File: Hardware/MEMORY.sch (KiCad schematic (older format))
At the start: 9 parts, among them J37 Micro_SD_Card, U20 M24C64-WDW6TP

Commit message: Fixed merge issues
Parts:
- renumbered J37 to J14, R41 to R24, R42 to R25, R43 to R26, R44 to R27, R45 to R28, R46 to R29, R47 to R30, U20 to U11
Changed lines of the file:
@@
 LIBS:contrib
 LIBS:valves
+LIBS:ZeroPilot-cache
 EELAYER 25 0
 EELAYER END
@@
 $EndDescr
 $Comp
-L GND #PWR43
+L GND #PWR036
 U 1 1 5920672F
 P 9150 2600
-F 0 "#PWR43" H 9150 2350 50  0001 C CNN
+F 0 "#PWR036" H 9150 2350 50  0001 C CNN
 F 1 "GND" H 9150 2450 50  0000 C CNN
 F 2 "" H 9150 2600 50  0001 C CNN
@@
 SD_CS
 $Comp
-L GND #PWR42
+L GND #PWR037
 U 1 1 592067B5
 P 7300 2400
-F 0 "#PWR42" H 7300 2150 50  0001 C CNN
+F 0 "#PWR037" H 7300 2150 50  0001 C CNN
 F 1 "GND" H 7300 2250 50  0000 C CNN
 F 2 "" H 7300 2400 50  0001 C CNN
@@
 $EndComp
 $Comp
-L GND #PWR41
+L GND #PWR038
 U 1 1 592069E4
 P 5150 5850
-F 0 "#PWR41" H 5150 5600 50  0001 C CNN
+F 0 "#PWR038" H 5150 5600 50  0001 C CNN
 F 1 "GND" H 5150 5700 50  0000 C CNN
 F 2 "" H 5150 5850 50  0001 C CNN
@@
 E3
 $Comp
-L R R42
+L R R25
 U 1 1 59206C6F
 P 1650 5650
-F 0 "R42" V 1730 5650 50  0000 C CNN
+F 0 "R25" V 1730 5650 50  0000 C CNN
 F 1 "10K" V 1650 5650 50  0000 C CNN
 F 2 "Resistors_SMD:R_0603_HandSoldering" V 1580 5650 50  0001 C CNN
@@
 $EndComp
 $Comp
-L R R41
+L R R24
 U 1 1 59206D63
 P 1650 5100
-F 0 "R41" V 1730 5100 50  0000 C CNN
+F 0 "R24" V 1730 5100 50  0000 C CNN
 F 1 "0" V 1650 5100 50  0000 C CNN
 F 2 "Resistors_SMD:R_0603_HandSoldering" V 1580 5100 50  0001 C CNN
@@
 $EndComp
 $Comp
-L GND #PWR40
+L GND #PWR039
 U 1 1 59206DDE
 P 1900 5950
-F 0 "#PWR40" H 1900 5700 50  0001 C CNN
+F 0 "#PWR039" H 1900 5700 50  0001 C CNN
 F 1 "GND" H 1900 5800 50  0000 C CNN
 F 2 "" H 1900 5950 50  0001 C CNN
@@
 NoConn ~ 7400 2300
 $Comp
-L Micro_SD_Card J37
+L Micro_SD_Card J14
 U 1 1 59517B7C
 P 8300 1900
-F 0 "J37" H 7650 2500 50  0000 C CNN
+F 0 "J14" H 7650 2500 50  0000 C CNN
 F 1 "Micro_SD_Card" H 8950 2500 50  0000 R CNN
 F 2 "WARG:micro_sd" H 9450 2200 50  0001 C CNN
@@
 $EndComp
 $Comp
-L R R44
+L R R27
 U 1 1 59596B34
 P 1900 5650
-F 0 "R44" V 1980 5650 50  0000 C CNN
+F 0 "R27" V 1980 5650 50  0000 C CNN
 F 1 "10K" V 1900 5650 50  0000 C CNN
 F 2 "Resistors_SMD:R_0603_HandSoldering" V 1830 5650 50  0001 C CNN
@@
 $EndComp
 $Comp
-L R R46
+L R R29
 U 1 1 59596B68
 P 2150 5650
-F 0 "R46" V 2230 5650 50  0000 C CNN
+F 0 "R29" V 2230 5650 50  0000 C CNN
 F 1 "10K" V 2150 5650 50  0000 C CNN
 F 2 "Resistors_SMD:R_0603_HandSoldering" V 2080 5650 50  0001 C CNN
@@
 $EndComp
 $Comp
-L R R43
+L R R26
 U 1 1 59596BE6
 P 1900 5100
-F 0 "R43" V 1980 5100 50  0000 C CNN
+F 0 "R26" V 1980 5100 50  0000 C CNN
 F 1 "0" V 1900 5100 50  0000 C CNN
 F 2 "Resistors_SMD:R_0603_HandSoldering" V 1830 5100 50  0001 C CNN
@@
 $EndComp
 $Comp
-L R R45
+L R R28
 U 1 1 59596C1A
 P 2150 5100
-F 0 "R45" V 2230 5100 50  0000 C CNN
+F 0 "R28" V 2230 5100 50  0000 C CNN
 F 1 "0" V 2150 5100 50  0000 C CNN
 F 2 "Resistors_SMD:R_0603_HandSoldering" V 2080 5100 50  0001 C CNN
@@
 $EndComp
 $Comp
-L R R47
+L R R30
 U 1 1 59596D32
 P 3950 5300
-F 0 "R47" V 4030 5300 50  0000 C CNN
+F 0 "R30" V 4030 5300 50  0000 C CNN
 F 1 "10K" V 3950 5300 50  0000 C CNN
 F 2 "Resistors_SMD:R_0603_HandSoldering" V 3880 5300 50  0001 C CNN
@@
 $EndComp
 $Comp
-L M24C64-WDW6TP U20
+L M24C64-WDW6TP U11
 U 1 1 595FB585
 P 5300 5000
-F 0 "U20" H 5300 5450 60  0000 C CNN
+F 0 "U11" H 5300 5450 60  0000 C CNN
 F 1 "M24C64-WDW6TP" H 5250 4100 60  0000 C CNN
 F 2 "Housings_SSOP:TSSOP-8_4.4x3mm_Pitch0.65mm" H 5200 5350 60  0001 C CNN

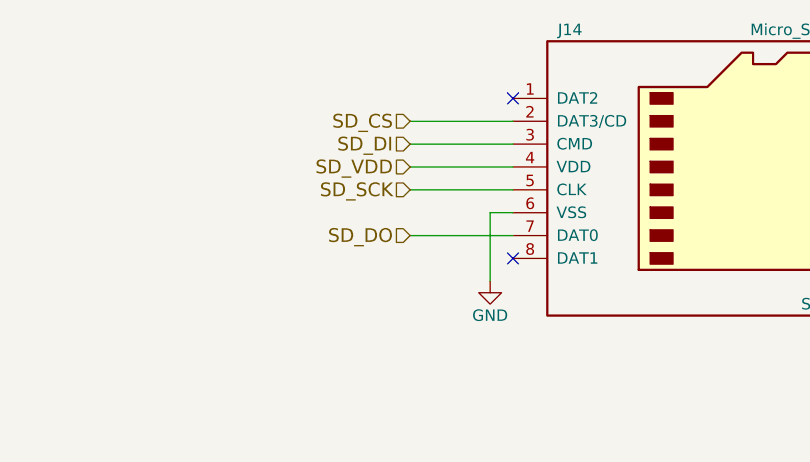
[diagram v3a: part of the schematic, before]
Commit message: Updated schematic
-Changed diode to 0603 diodes
-Changed SD card to proper pinout
-Fixed SPI1 conflict
-Renamed some power nets
-Fixed naming error in IMU NSS
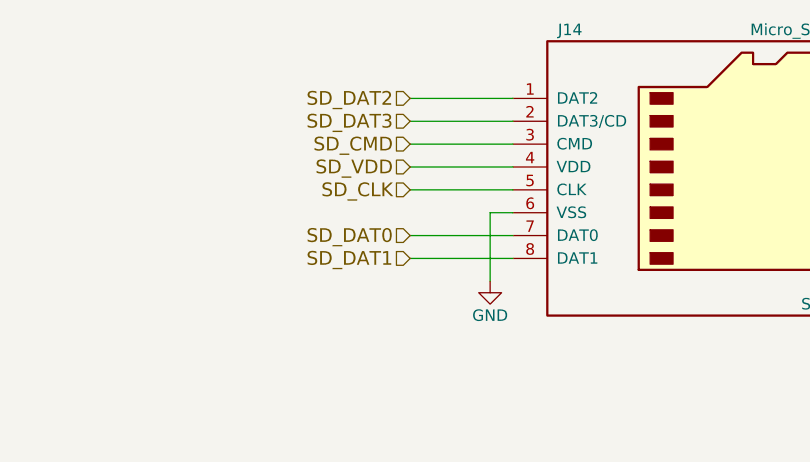
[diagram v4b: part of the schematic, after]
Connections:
- net labels added: SD_CLK, SD_CMD, SD_DAT0, SD_DAT1, SD_DAT2, SD_DAT3
- net labels removed: SD_CS, SD_DI, SD_DO, SD_SCK
- wire segments 28 -> 30
- no-connect marks 2 -> 0
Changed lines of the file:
@@
 $EndComp
 Text HLabel 6950 1800 0    60   Input ~ 0
-SD_DI
+SD_CMD
 Text HLabel 6950 2200 0    60   Input ~ 0
-SD_DO
+SD_DAT0
 Text HLabel 6950 2000 0    60   Input ~ 0
-SD_SCK
+SD_CLK
 Text HLabel 6950 1900 0    60   Input ~ 0
 SD_VDD
 Text HLabel 6950 1700 0    60   Input ~ 0
-SD_CS
+SD_DAT3
 $Comp
 L GND #PWR037
@@
 Text Notes 1250 4650 0    60   ~ 0
 Populate resistors to select I2C address\n
-NoConn ~ 7400 1600
-NoConn ~ 7400 2300
 $Comp
 L Micro_SD_Card J14
@@
 Text HLabel 3850 5500 0    60   Input ~ 0
 WC
+Wire Wire Line
+	7400 2300 6950 2300
+Text HLabel 6950 2300 0    60   Input ~ 0
+SD_DAT1
+Text HLabel 6950 1600 0    60   Input ~ 0
+SD_DAT2
+Wire Wire Line
+	6950 1600 7400 1600
 $EndSCHEMATC

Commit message: Remapped symbols for KiCAD 5.0.x
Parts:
- J14: symbol Micro_SD_Card -> conn:Micro_SD_Card
- R24, R25, R26, R27, R28, R29, R30: symbol R -> Device:R
- U11: symbol M24C64-WDW6TP -> WARG:M24C64-WDW6TP
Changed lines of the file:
@@
-EESchema Schematic File Version 2
-LIBS:WARG
-LIBS:power
-LIBS:device
-LIBS:transistors
-LIBS:conn
-LIBS:linear
-LIBS:regul
-LIBS:74xx
-LIBS:cmos4000
-LIBS:adc-dac
-LIBS:memory
-LIBS:xilinx
-LIBS:microcontrollers
-LIBS:dsp
-LIBS:microchip
-LIBS:analog_switches
-LIBS:motorola
-LIBS:texas
-LIBS:intel
-LIBS:audio
-LIBS:interface
-LIBS:digital-audio
-LIBS:philips
-LIBS:display
-LIBS:cypress
-LIBS:siliconi
-LIBS:opto
-LIBS:atmel
-LIBS:contrib
-LIBS:valves
+EESchema Schematic File Version 4
 LIBS:ZeroPilot-cache
-EELAYER 25 0
+EELAYER 26 0
 EELAYER END
 $Descr A4 11693 8268
@@
 $EndDescr
 $Comp
-L GND #PWR036
+L power:GND #PWR036
 U 1 1 5920672F
 P 9150 2600
@@
 SD_DAT3
 $Comp
-L GND #PWR037
+L power:GND #PWR037
 U 1 1 592067B5
 P 7300 2400
@@
 $EndComp
 $Comp
-L GND #PWR038
+L power:GND #PWR038
 U 1 1 592069E4
 P 5150 5850
@@
 E3
 $Comp
-L R R25
+L Device:R R25
 U 1 1 59206C6F
 P 1650 5650
@@
 $EndComp
 $Comp
-L R R24
+L Device:R R24
 U 1 1 59206D63
 P 1650 5100
@@
 $EndComp
 $Comp
-L GND #PWR039
+L power:GND #PWR039
 U 1 1 59206DDE
 P 1900 5950
@@
 Populate resistors to select I2C address\n
 $Comp
-L Micro_SD_Card J14
+L conn:Micro_SD_Card J14
 U 1 1 59517B7C
 P 8300 1900
@@
 $EndComp
 $Comp
-L R R27
+L Device:R R27
 U 1 1 59596B34
 P 1900 5650
@@
 $EndComp
 $Comp
-L R R29
+L Device:R R29
 U 1 1 59596B68
 P 2150 5650
@@
 $EndComp
 $Comp
-L R R26
+L Device:R R26
 U 1 1 59596BE6
 P 1900 5100
@@
 $EndComp
 $Comp
-L R R28
+L Device:R R28
 U 1 1 59596C1A
 P 2150 5100
@@
 $EndComp
 $Comp
-L R R30
+L Device:R R30
 U 1 1 59596D32
 P 3950 5300
@@
 $EndComp
 $Comp
-L M24C64-WDW6TP U11
+L WARG:M24C64-WDW6TP U11
 U 1 1 595FB585
 P 5300 5000
@@
 	5550 5350 5750 5350
 Wire Wire Line
-	3850 5500 4650 5500
+	3850 5500 3950 5500
 Wire Wire Line
 	3950 5450 3950 5500
@@
 	1650 5800 1650 5900
 Wire Wire Line
-	1650 5900 2150 5900
+	1650 5900 1900 5900
 Wire Wire Line
 	2150 5900 2150 5800
 Wire Wire Line
-	1900 5800 1900 5950
+	1900 5800 1900 5900
 Connection ~ 1900 5900
 Wire Wire Line
-	1650 4800 2150 4800
+	1650 4800 1900 4800
 Wire Wire Line
 	1650 4800 1650 4950
@@
 Wire Wire Line
 	6950 1600 7400 1600
+Wire Wire Line
+	3950 5500 4650 5500
+Wire Wire Line
+	1900 5900 2150 5900
+Wire Wire Line
+	1900 5900 1900 5950
+Wire Wire Line
+	1900 4800 2150 4800
 $EndSCHEMATC

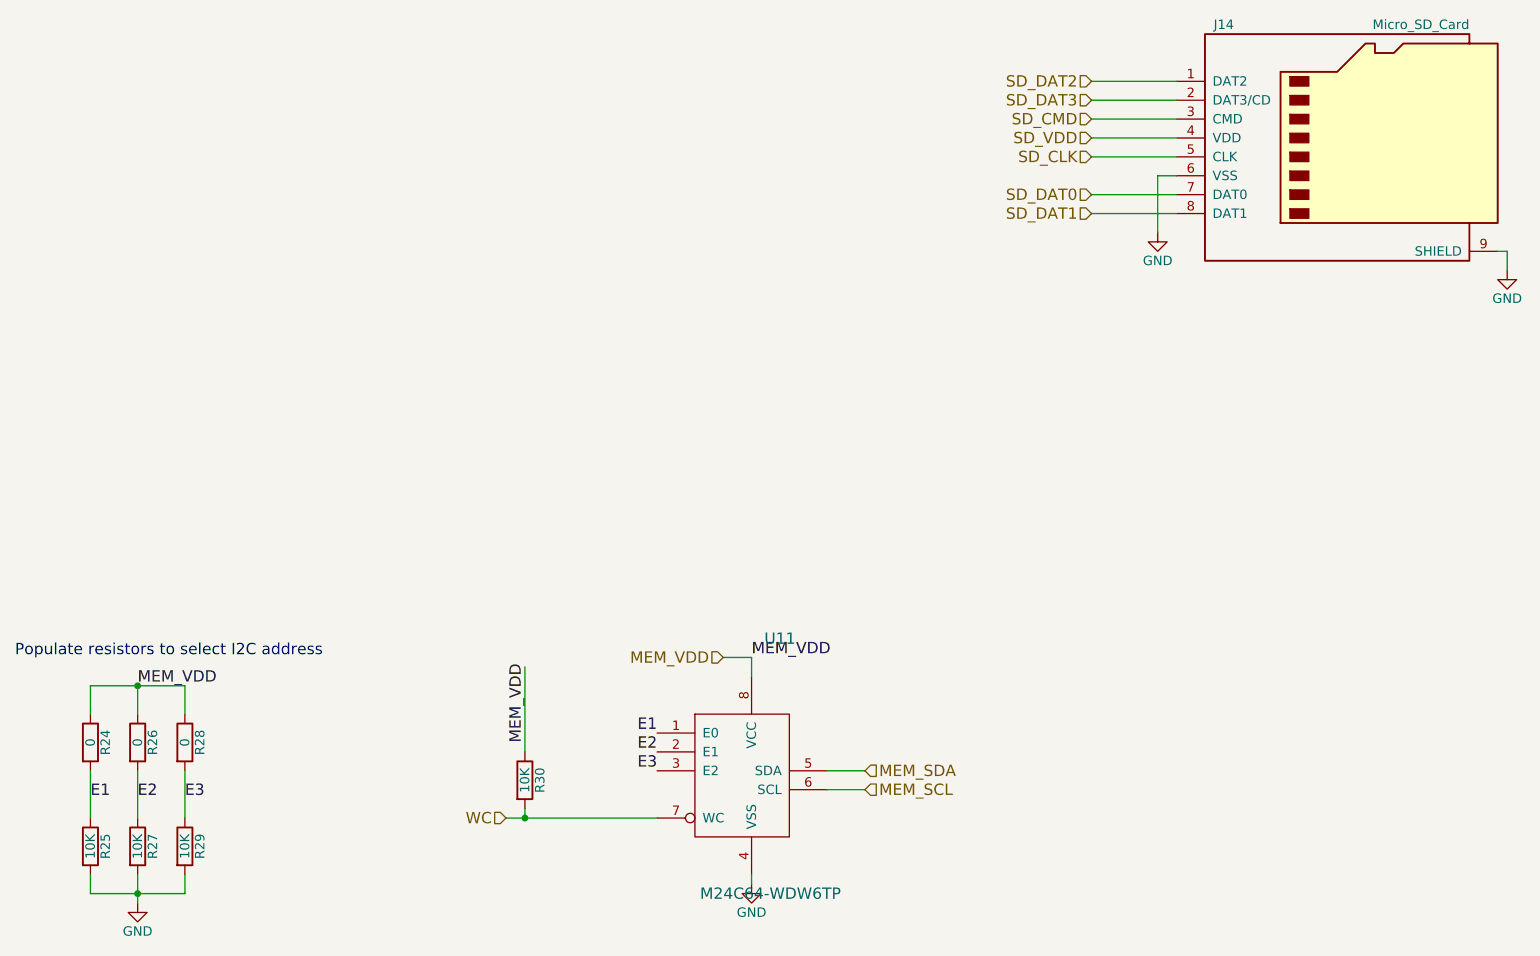
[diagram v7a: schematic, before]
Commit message: Generated netlist and board outline
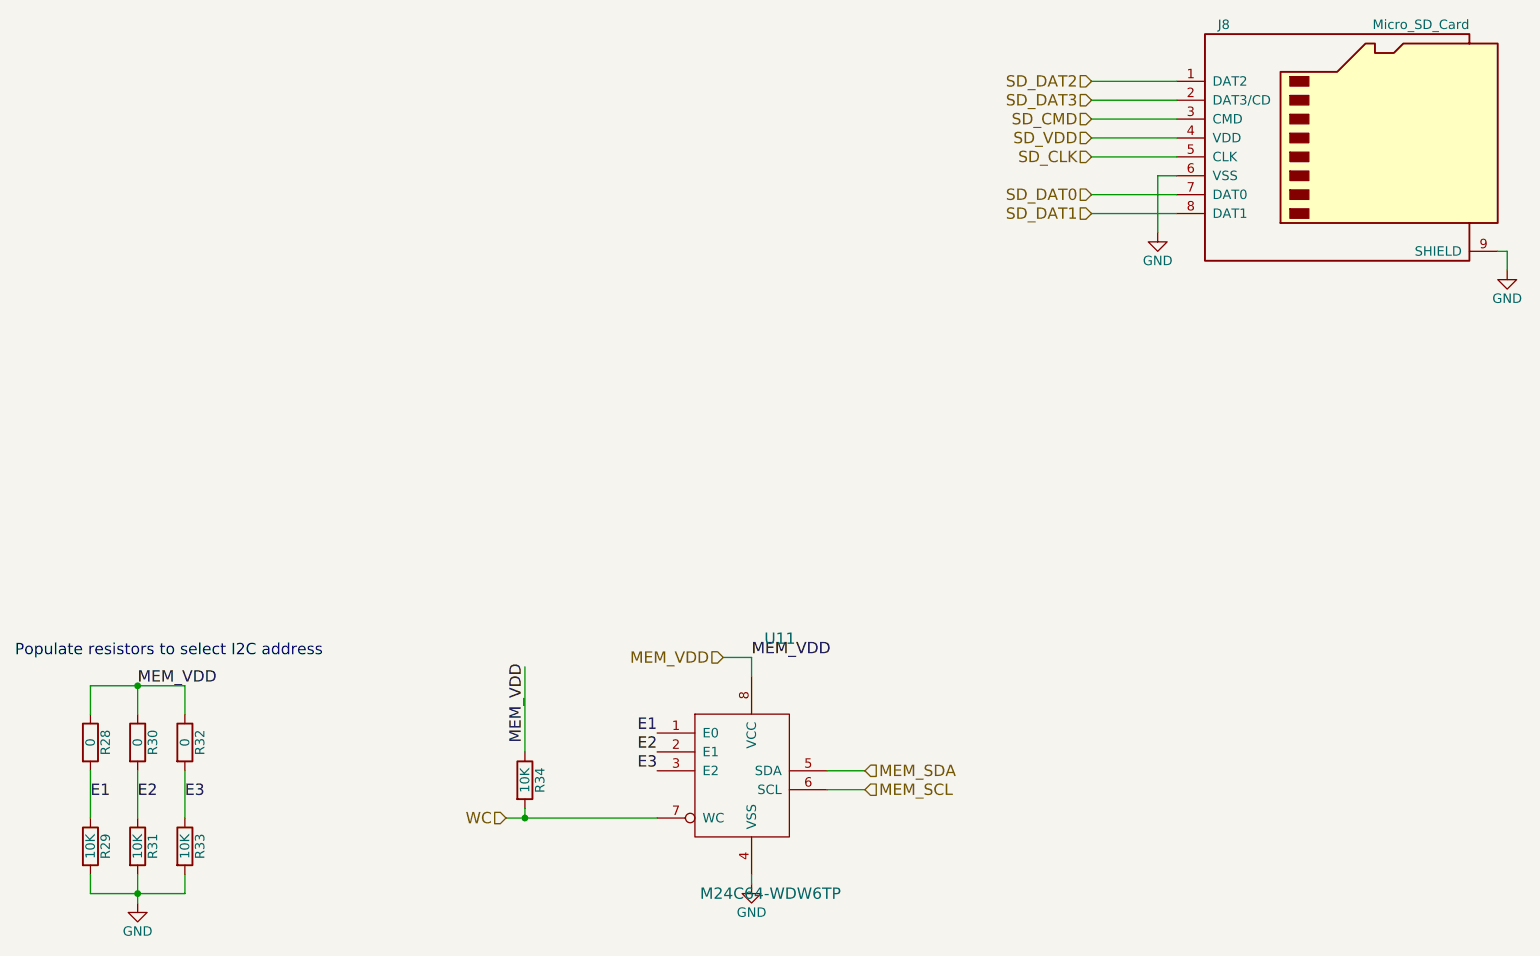
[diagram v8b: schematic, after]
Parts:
- renumbered J14 to J8, R24 to R28, R25 to R29, R26 to R30, R27 to R31, R28 to R32, R29 to R33, R30 to R34
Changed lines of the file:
@@
 $EndDescr
 $Comp
-L power:GND #PWR036
+L power:GND #PWR040
 U 1 1 5920672F
 P 9150 2600
-F 0 "#PWR036" H 9150 2350 50  0001 C CNN
+F 0 "#PWR040" H 9150 2350 50  0001 C CNN
 F 1 "GND" H 9150 2450 50  0000 C CNN
 F 2 "" H 9150 2600 50  0001 C CNN
@@
 SD_DAT3
 $Comp
-L power:GND #PWR037
+L power:GND #PWR039
 U 1 1 592067B5
 P 7300 2400
-F 0 "#PWR037" H 7300 2150 50  0001 C CNN
+F 0 "#PWR039" H 7300 2150 50  0001 C CNN
 F 1 "GND" H 7300 2250 50  0000 C CNN
 F 2 "" H 7300 2400 50  0001 C CNN
@@
 E3
 $Comp
-L Device:R R25
+L Device:R R29
 U 1 1 59206C6F
 P 1650 5650
-F 0 "R25" V 1730 5650 50  0000 C CNN
+F 0 "R29" V 1730 5650 50  0000 C CNN
 F 1 "10K" V 1650 5650 50  0000 C CNN
 F 2 "Resistors_SMD:R_0603_HandSoldering" V 1580 5650 50  0001 C CNN
@@
 $EndComp
 $Comp
-L Device:R R24
+L Device:R R28
 U 1 1 59206D63
 P 1650 5100
-F 0 "R24" V 1730 5100 50  0000 C CNN
+F 0 "R28" V 1730 5100 50  0000 C CNN
 F 1 "0" V 1650 5100 50  0000 C CNN
 F 2 "Resistors_SMD:R_0603_HandSoldering" V 1580 5100 50  0001 C CNN
@@
 $EndComp
 $Comp
-L power:GND #PWR039
+L power:GND #PWR037
 U 1 1 59206DDE
 P 1900 5950
-F 0 "#PWR039" H 1900 5700 50  0001 C CNN
+F 0 "#PWR037" H 1900 5700 50  0001 C CNN
 F 1 "GND" H 1900 5800 50  0000 C CNN
 F 2 "" H 1900 5950 50  0001 C CNN
@@
 Populate resistors to select I2C address\n
 $Comp
-L conn:Micro_SD_Card J14
+L conn:Micro_SD_Card J8
 U 1 1 59517B7C
 P 8300 1900
-F 0 "J14" H 7650 2500 50  0000 C CNN
+F 0 "J8" H 7650 2500 50  0000 C CNN
 F 1 "Micro_SD_Card" H 8950 2500 50  0000 R CNN
 F 2 "WARG:micro_sd" H 9450 2200 50  0001 C CNN
@@
 $EndComp
 $Comp
-L Device:R R27
+L Device:R R31
 U 1 1 59596B34
 P 1900 5650
-F 0 "R27" V 1980 5650 50  0000 C CNN
+F 0 "R31" V 1980 5650 50  0000 C CNN
 F 1 "10K" V 1900 5650 50  0000 C CNN
 F 2 "Resistors_SMD:R_0603_HandSoldering" V 1830 5650 50  0001 C CNN
@@
 $EndComp
 $Comp
-L Device:R R29
+L Device:R R33
 U 1 1 59596B68
 P 2150 5650
-F 0 "R29" V 2230 5650 50  0000 C CNN
+F 0 "R33" V 2230 5650 50  0000 C CNN
 F 1 "10K" V 2150 5650 50  0000 C CNN
 F 2 "Resistors_SMD:R_0603_HandSoldering" V 2080 5650 50  0001 C CNN
@@
 $EndComp
 $Comp
-L Device:R R26
+L Device:R R30
 U 1 1 59596BE6
 P 1900 5100
-F 0 "R26" V 1980 5100 50  0000 C CNN
+F 0 "R30" V 1980 5100 50  0000 C CNN
 F 1 "0" V 1900 5100 50  0000 C CNN
 F 2 "Resistors_SMD:R_0603_HandSoldering" V 1830 5100 50  0001 C CNN
@@
 $EndComp
 $Comp
-L Device:R R28
+L Device:R R32
 U 1 1 59596C1A
 P 2150 5100
-F 0 "R28" V 2230 5100 50  0000 C CNN
+F 0 "R32" V 2230 5100 50  0000 C CNN
 F 1 "0" V 2150 5100 50  0000 C CNN
 F 2 "Resistors_SMD:R_0603_HandSoldering" V 2080 5100 50  0001 C CNN
@@
 $EndComp
 $Comp
-L Device:R R30
+L Device:R R34
 U 1 1 59596D32
 P 3950 5300
-F 0 "R30" V 4030 5300 50  0000 C CNN
+F 0 "R34" V 4030 5300 50  0000 C CNN
 F 1 "10K" V 3950 5300 50  0000 C CNN
 F 2 "Resistors_SMD:R_0603_HandSoldering" V 3880 5300 50  0001 C CNN
